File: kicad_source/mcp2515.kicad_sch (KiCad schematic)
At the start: 14 parts, among them CN4 GH_SM04B-GHS-TB, CN5 GH_SM04B-GHS-TB, U8 MCP2515, U9 SN65HVD232, Y1 16MHz

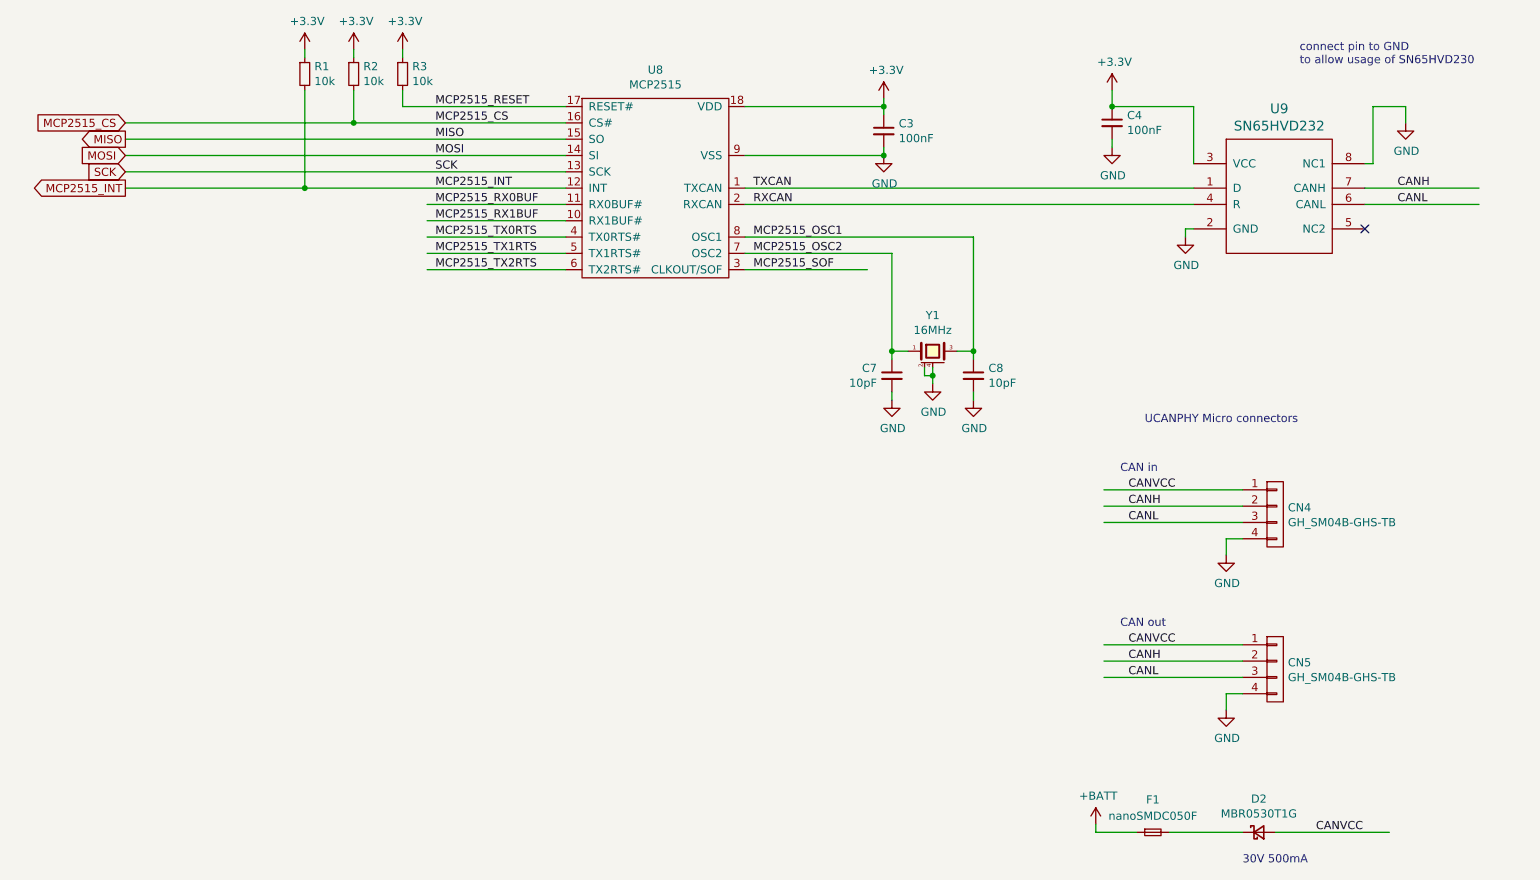
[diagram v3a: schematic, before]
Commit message: clearified some part numbers
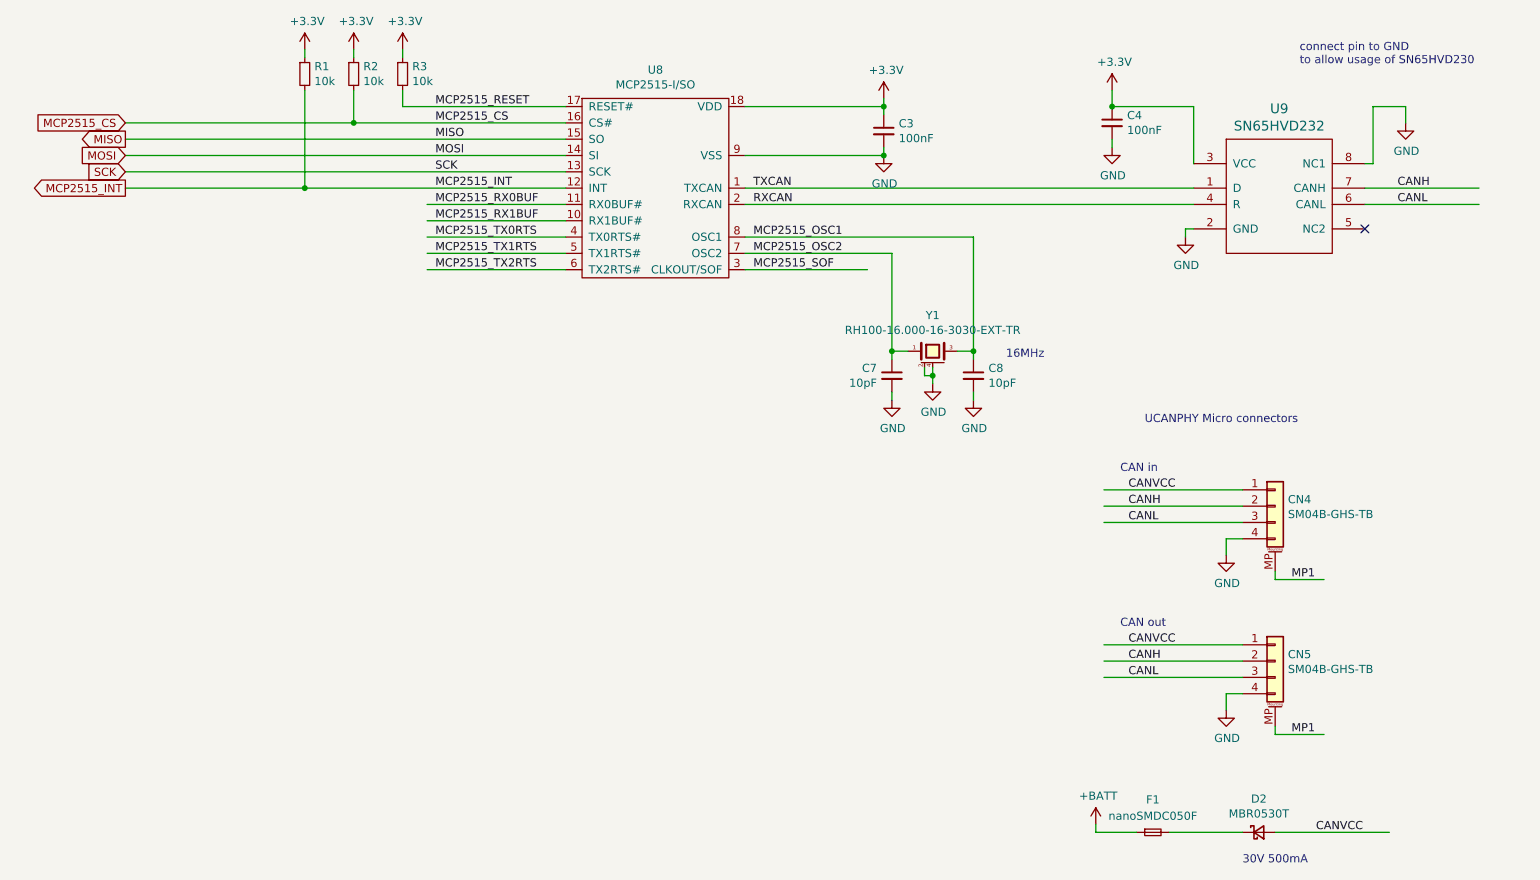
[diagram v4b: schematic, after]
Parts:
- CN4, CN5: value GH_SM04B-GHS-TB -> SM04B-GHS-TB; symbol OpenCyphalPicoBase-rescue:CONN_01X04-mechanical-connectors -> Connector_Generic_MountingPin:Conn_01x04_MountingPin
- D2: value MBR0530T1G -> MBR0530T
- U8: value MCP2515 -> MCP2515-I/SO
- Y1: value 16MHz -> RH100-16.000-16-3030-EXT-TR
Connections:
- new net MP1: CN4.MP (MountPin), CN5.MP (MountPin)
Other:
- note added: "16MHz"
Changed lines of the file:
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@@
+    (stroke (width 0) (type default) (color 0 0 0 0))
+  )
+  (wire (pts (xy 231.14 116.84) (xy 223.52 116.84))
     (stroke (width 0) (type default) (color 0 0 0 0))
   )
@@
     (stroke (width 0) (type default) (color 0 0 0 0))
   )
+  (wire (pts (xy 223.52 116.84) (xy 223.52 115.57))
+    (stroke (width 0) (type default) (color 0 0 0 0))
+  )
+  (wire (pts (xy 223.52 140.97) (xy 223.52 139.7))
+    (stroke (width 0) (type default) (color 0 0 0 0))
+  )
   (wire (pts (xy 91.44 58.42) (xy 113.03 58.42))
     (stroke (width 0) (type default) (color 0 0 0 0))
@@
     (stroke (width 0) (type default) (color 0 0 0 0))
   )
+  (wire (pts (xy 231.14 140.97) (xy 223.52 140.97))
+    (stroke (width 0) (type default) (color 0 0 0 0))
+  )
   (wire (pts (xy 72.39 40.64) (xy 72.39 55.88))
     (stroke (width 0) (type default) (color 0 0 0 0))
@@
     (stroke (width 0) (type default) (color 0 0 0 0))
   )
+  (text "16MHz" (at 181.61 82.55 0)
+    (effects (font (size 1.27 1.27)) (justify left bottom))
+  )
   (text "connect pin to GND\nto allow usage of SN65HVD230" (at 227.33 36.83 0)
     (effects (font (size 1.27 1.27)) (justify left bottom))
@@
     (effects (font (size 1.27 1.27)) (justify left bottom))
   )
+  (label "MP1" (at 226.06 116.84 0)
+    (effects (font (size 1.27 1.27)) (justify left bottom))
+  )
   (label "MCP2515_CS" (at 92.71 45.72 0)
     (effects (font (size 1.27 1.27)) (justify left bottom))
@@
   )
   (label "MOSI" (at 92.71 50.8 0)
+    (effects (font (size 1.27 1.27)) (justify left bottom))
+  )
+  (label "MP1" (at 226.06 140.97 0)
     (effects (font (size 1.27 1.27)) (justify left bottom))
   )
@@
     (in_bom yes) (on_board yes)
     (property "Reference" "U8" (id 0) (at 127 37.465 0))
-    (property "Value" "MCP2515" (id 1) (at 127 39.7764 0))
+    (property "Value" "MCP2515-I/SO" (id 1) (at 127 39.7764 0))
     (property "Footprint" "Package_SO:SOIC-18W_7.5x11.6mm_P1.27mm" (id 2) (at 127 55.88 0)
       (effects (font (size 1.27 1.27)) hide)
@@
     (in_bom yes) (on_board yes)
     (property "Reference" "Y1" (id 0) (at 170.18 75.692 0))
-    (property "Value" "16MHz" (id 1) (at 170.18 78.0034 0))
+    (property "Value" "RH100-16.000-16-3030-EXT-TR" (id 1) (at 170.18 78.0034 0))
     (property "Footprint" "crystals:Crystal_SMD_3.2x2.5mm_4Pad" (id 2) (at 170.18 86.36 0)
       (effects (font (size 1.27 1.27)) hide)
@@
     (pin "1")
   )
-  (symbol (lib_id "OpenCyphalPicoBase-rescue:CONN_01X04-mechanical-connectors") (at 223.52 106.68 0) (unit 1)
-    (in_bom yes) (on_board yes)
-    (property "Reference" "CN4" (id 0) (at 225.5012 105.6386 0)
-      (effects (font (size 1.27 1.27)) (justify left))
-    )
-    (property "Value" "GH_SM04B-GHS-TB" (id 1) (at 225.5012 107.95 0)
-      (effects (font (size 1.27 1.27)) (justify left))
-    )
-    (property "Footprint" "Connector_JST:JST_GH_SM04B-GHS-TB_1x04-1MP_P1.25mm_Horizontal" (id 2) (at 223.52 106.68 0)
-      (effects (font (size 1.27 1.27)) hide)
-    )
-    (property "Datasheet" "" (id 3) (at 223.52 106.68 0))
+  (symbol (lib_id "Connector_Generic_MountingPin:Conn_01x04_MountingPin") (at 223.52 105.41 0) (unit 1)
+    (in_bom yes) (on_board yes)
+    (property "Reference" "CN4" (id 0) (at 225.5012 104.3686 0)
+      (effects (font (size 1.27 1.27)) (justify left))
+    )
+    (property "Value" "SM04B-GHS-TB" (id 1) (at 225.5012 106.68 0)
+      (effects (font (size 1.27 1.27)) (justify left))
+    )
+    (property "Footprint" "Connector_JST:JST_GH_SM04B-GHS-TB_1x04-1MP_P1.25mm_Horizontal" (id 2) (at 223.52 105.41 0)
+      (effects (font (size 1.27 1.27)) hide)
+    )
+    (property "Datasheet" "~" (id 3) (at 223.52 105.41 0)
+      (effects (font (size 1.27 1.27)) hide)
+    )
     (pin "1")
     (pin "2")
     (pin "3")
     (pin "4")
+    (pin "MP")
   )
   (symbol (lib_id "OpenCyphalPicoBase-rescue:GND-power-supply") (at 215.9 113.03 0) (unit 1)
@@
     (pin "1")
   )
-  (symbol (lib_id "OpenCyphalPicoBase-rescue:CONN_01X04-mechanical-connectors") (at 223.52 130.81 0) (unit 1)
-    (in_bom yes) (on_board yes)
-    (property "Reference" "CN5" (id 0) (at 225.5012 129.7686 0)
-      (effects (font (size 1.27 1.27)) (justify left))
-    )
-    (property "Value" "GH_SM04B-GHS-TB" (id 1) (at 225.5012 132.08 0)
-      (effects (font (size 1.27 1.27)) (justify left))
-    )
-    (property "Footprint" "Connector_JST:JST_GH_SM04B-GHS-TB_1x04-1MP_P1.25mm_Horizontal" (id 2) (at 223.52 130.81 0)
-      (effects (font (size 1.27 1.27)) hide)
-    )
-    (property "Datasheet" "" (id 3) (at 223.52 130.81 0))
+  (symbol (lib_id "Connector_Generic_MountingPin:Conn_01x04_MountingPin") (at 223.52 129.54 0) (unit 1)
+    (in_bom yes) (on_board yes)
+    (property "Reference" "CN5" (id 0) (at 225.5012 128.4986 0)
+      (effects (font (size 1.27 1.27)) (justify left))
+    )
+    (property "Value" "SM04B-GHS-TB" (id 1) (at 225.5012 130.81 0)
+      (effects (font (size 1.27 1.27)) (justify left))
+    )
+    (property "Footprint" "Connector_JST:JST_GH_SM04B-GHS-TB_1x04-1MP_P1.25mm_Horizontal" (id 2) (at 223.52 129.54 0)
+      (effects (font (size 1.27 1.27)) hide)
+    )
+    (property "Datasheet" "~" (id 3) (at 223.52 129.54 0)
+      (effects (font (size 1.27 1.27)) hide)
+    )
     (pin "1")
     (pin "2")
     (pin "3")
     (pin "4")
+    (pin "MP")
   )
   (symbol (lib_id "OpenCyphalPicoBase-rescue:GND-power-supply") (at 215.9 137.16 0) (unit 1)
@@
     (in_bom yes) (on_board yes)
     (property "Reference" "D2" (id 0) (at 220.98 151.003 0))
-    (property "Value" "MBR0530T1G" (id 1) (at 220.98 153.3144 0))
+    (property "Value" "MBR0530T" (id 1) (at 220.98 153.3144 0))
     (property "Footprint" "Diode_SMD:D_SOD-123" (id 2) (at 220.98 156.21 90)
       (effects (font (size 1.27 1.27)) hide)

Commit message: added some JLCPCB part numbers and BOM
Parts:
- C3, C4: LCSC (none) -> C314282
- C7, C8: LCSC (none) -> C91367
- CN4, CN5: LCSC (none) -> C189895
- D2: LCSC (none) -> C77336
- R1, R2, R3: LCSC (none) -> C3152123
- U8: value MCP2515-I/SO -> MCP2515T-I/SO; LCSC (none) -> C153782
- U9: LCSC (none) -> C30530
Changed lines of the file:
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@@
     (in_bom yes) (on_board yes)
     (property "Reference" "U8" (id 0) (at 127 37.465 0))
-    (property "Value" "MCP2515-I/SO" (id 1) (at 127 39.7764 0))
+    (property "Value" "MCP2515T-I/SO" (id 1) (at 127 39.7764 0))
     (property "Footprint" "Package_SO:SOIC-18W_7.5x11.6mm_P1.27mm" (id 2) (at 127 55.88 0)
       (effects (font (size 1.27 1.27)) hide)
     )
     (property "Datasheet" "" (id 3) (at 127 55.88 0)
+      (effects (font (size 1.27 1.27)) hide)
+    )
+    (property "LCSC" "C153782" (id 4) (at 127 55.88 0)
       (effects (font (size 1.27 1.27)) hide)
     )
@@
     )
     (property "Datasheet" "" (id 3) (at 162.56 46.99 0))
+    (property "LCSC" "C314282" (id 4) (at 162.56 46.99 0)
+      (effects (font (size 1.27 1.27)) hide)
+    )
     (pin "1")
     (pin "2")
@@
     )
     (property "Datasheet" "" (id 3) (at 87.63 38.1 0))
+    (property "LCSC" "C3152123" (id 4) (at 87.63 38.1 0)
+      (effects (font (size 1.27 1.27)) hide)
+    )
     (pin "1")
     (pin "2")
@@
     )
     (property "Datasheet" "" (id 3) (at 80.01 38.1 0))
+    (property "LCSC" "C3152123" (id 4) (at 80.01 38.1 0)
+      (effects (font (size 1.27 1.27)) hide)
+    )
     (pin "1")
     (pin "2")
@@
     )
     (property "Datasheet" "" (id 3) (at 72.39 38.1 0))
+    (property "LCSC" "C3152123" (id 4) (at 72.39 38.1 0)
+      (effects (font (size 1.27 1.27)) hide)
+    )
     (pin "1")
     (pin "2")
@@
     (property "Datasheet" "" (id 3) (at 210.82 62.23 0)
       (effects (font (size 1.524 1.524)))
+    )
+    (property "LCSC" "C30530" (id 4) (at 210.82 66.04 0)
+      (effects (font (size 1.27 1.27)) hide)
     )
     (pin "1")
@@
     )
     (property "Datasheet" "" (id 3) (at 198.12 45.72 0))
+    (property "LCSC" "C314282" (id 4) (at 198.12 45.72 0)
+      (effects (font (size 1.27 1.27)) hide)
+    )
     (pin "1")
     (pin "2")
@@
       (effects (font (size 1.27 1.27)) hide)
     )
+    (property "LCSC" "C189895" (id 4) (at 223.52 105.41 0)
+      (effects (font (size 1.27 1.27)) hide)
+    )
     (pin "1")
     (pin "2")
@@
       (effects (font (size 1.27 1.27)) hide)
     )
+    (property "LCSC" "C189895" (id 4) (at 223.52 129.54 0)
+      (effects (font (size 1.27 1.27)) hide)
+    )
     (pin "1")
     (pin "2")
@@
     )
     (property "Datasheet" "" (id 3) (at 220.98 156.21 90))
+    (property "LCSC" "C77336" (id 4) (at 220.98 156.21 0)
+      (effects (font (size 1.27 1.27)) hide)
+    )
     (pin "1")
     (pin "2")
@@
     )
     (property "Datasheet" "" (id 3) (at 176.53 85.09 0))
+    (property "LCSC" "C91367" (id 4) (at 176.53 85.09 0)
+      (effects (font (size 1.27 1.27)) hide)
+    )
     (pin "1")
     (pin "2")
@@
     )
     (property "Datasheet" "" (id 3) (at 163.83 85.09 0))
-    (pin "1")
-    (pin "2")
+    (property "LCSC" "C91367" (id 4) (at 163.83 85.09 0)
+      (effects (font (size 1.27 1.27)) hide)
+    )
+    (pin "1")
+    (pin "2")

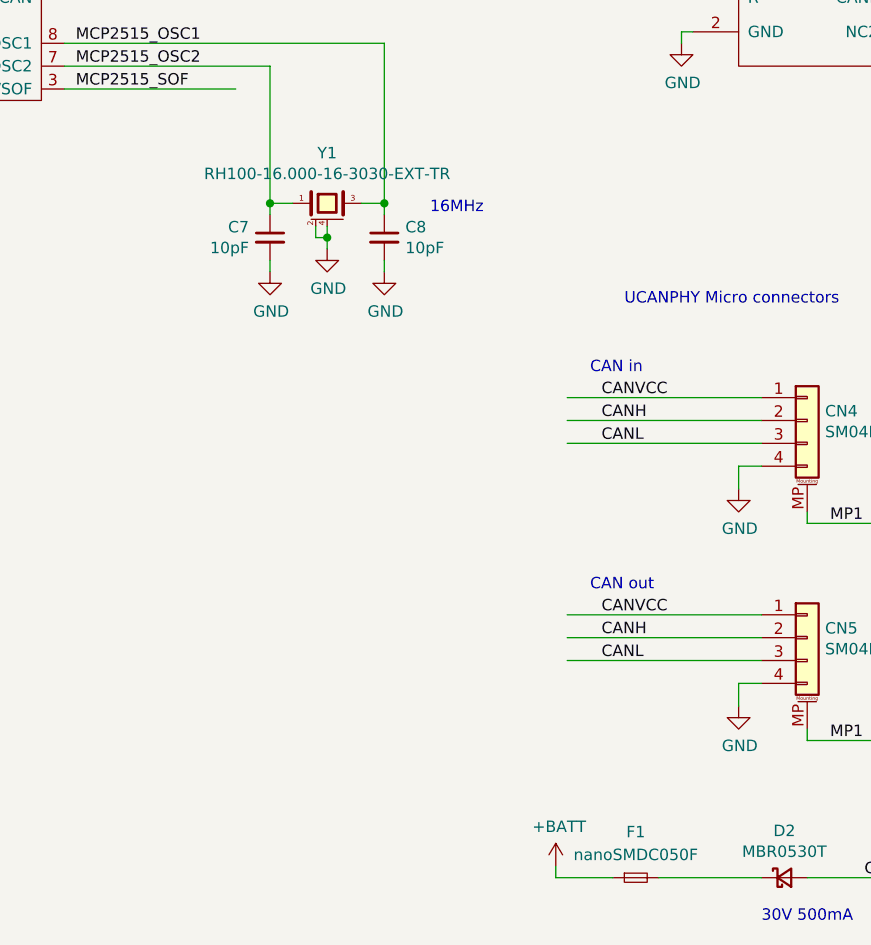
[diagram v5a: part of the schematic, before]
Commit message: added missing JLCPCB part numbers
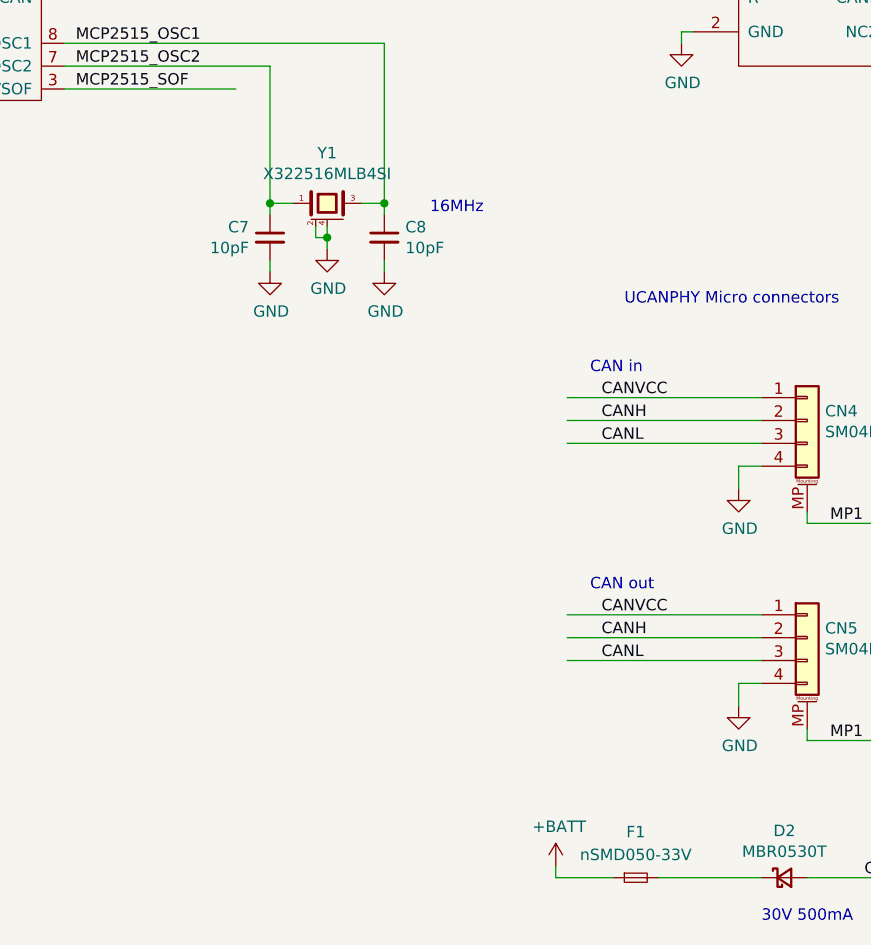
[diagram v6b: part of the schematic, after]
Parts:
- F1: value nanoSMDC050F -> nSMD050-33V; LCSC (none) -> C70077
- Y1: value RH100-16.000-16-3030-EXT-TR -> X322516MLB4SI; LCSC (none) -> C13738
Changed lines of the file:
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@@
     (in_bom yes) (on_board yes)
     (property "Reference" "Y1" (id 0) (at 170.18 75.692 0))
-    (property "Value" "RH100-16.000-16-3030-EXT-TR" (id 1) (at 170.18 78.0034 0))
+    (property "Value" "X322516MLB4SI" (id 1) (at 170.18 78.0034 0))
     (property "Footprint" "crystals:Crystal_SMD_3.2x2.5mm_4Pad" (id 2) (at 170.18 86.36 0)
       (effects (font (size 1.27 1.27)) hide)
     )
     (property "Datasheet" "" (id 3) (at 170.18 81.28 0))
+    (property "LCSC" "C13738" (id 4) (at 170.18 81.28 0)
+      (effects (font (size 1.27 1.27)) hide)
+    )
     (pin "1")
     (pin "2")
@@
     (in_bom yes) (on_board yes) (fields_autoplaced)
     (property "Reference" "F1" (id 0) (at 204.47 151.13 0))
-    (property "Value" "nanoSMDC050F" (id 1) (at 204.47 153.67 0))
+    (property "Value" "nSMD050-33V" (id 1) (at 204.47 153.67 0))
     (property "Footprint" "Fuse:Fuse_1206_3216Metric" (id 2) (at 204.47 156.21 0)
       (effects (font (size 1.27 1.27)) hide)
@@
       (effects (font (size 1.27 1.27)) hide)
     )
+    (property "LCSC" "C70077" (id 4) (at 204.47 156.21 0)
+      (effects (font (size 1.27 1.27)) hide)
+    )
